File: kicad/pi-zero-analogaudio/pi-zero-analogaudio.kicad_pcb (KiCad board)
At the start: 2 copper layers, 30.5 x 26 mm, 11 parts, among them J2 Pi Connector 2x5 Female, J3 Audio Out, U1 STX-3120-3B

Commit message: drilling holes, silk-screen print
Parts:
- added H1: MountingHole, MountingHole:MountingHole_2.7mm_M2.5_DIN965, F.Cu at (90.5, 62.5)
- added H2: MountingHole, MountingHole:MountingHole_2.7mm_M2.5_DIN965, F.Cu at (114.0, 62.5)
- U1: footprint STX-3120 -> Download:STX-3120
- moved U1 1.28 mm to (114.2, 72.4)
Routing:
- net Net-(C4-Pad2): track 19.9 -> 17.0 mm
- net Net-(C2-Pad2): track 32.5 -> 31.3 mm
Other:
- board text added: "G"
- board text added: "L"
- board text added: "Pi-Zero Audio Rev 6"
- board text added: "R"
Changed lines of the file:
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@@
   (general
     (thickness 1.6)
-    (drawings 4)
-    (tracks 37)
+    (drawings 8)
+    (tracks 35)
     (zones 0)
-    (modules 11)
+    (modules 13)
     (nets 14)
   )
@@
     (add_net "Net-(J2-Pad8)")
     (add_net "Net-(J2-Pad9)")
+  )
+  (module Download:STX-3120 (layer F.Cu)
+    (at 114.2 72.4 180)
+    (fp_text reference U1 (at 0 0) (layer F.SilkS)
+      (effects (font (size 0.787402 0.787402) (thickness 0.015)))
+    )
+    (fp_text value STX-3120-3B (at 0 0) (layer F.Fab)
+      (effects (font (size 0.787402 0.787402) (thickness 0.015)))
+    )
+    (fp_line (start -3 3.4) (end -3 -3.4) (layer F.Fab) (width 0.127))
+    (fp_line (start -6.5 3.4) (end -3 3.4) (layer F.Fab) (width 0.127))
+    (fp_line (start -6.5 -3.4) (end -6.5 3.4) (layer F.Fab) (width 0.127))
+    (fp_line (start -3 -3.4) (end -6.5 -3.4) (layer F.Fab) (width 0.127))
+    (fp_line (start -3 6) (end -3 -6) (layer F.SilkS) (width 0.127))
+    (fp_line (start 8.6 6) (end -3 6) (layer F.SilkS) (width 0.127))
+    (fp_line (start 8.6 -6) (end 8.6 6) (layer F.SilkS) (width 0.127))
+    (fp_line (start -3 -6) (end 8.6 -6) (layer F.SilkS) (width 0.127))
+    (pad None np_thru_hole circle (at 5 0 180) (size 1.6 1.6) (drill 1.6) (layers *.Cu *.Mask))
+    (pad None np_thru_hole circle (at 0 5 180) (size 1.6 1.6) (drill 1.6) (layers *.Cu *.Mask))
+    (pad None np_thru_hole circle (at 0 -5 180) (size 1.6 1.6) (drill 1.6) (layers *.Cu *.Mask))
+    (pad 2 thru_hole circle (at 5 5 180) (size 2.1844 2.1844) (drill 1.3) (layers *.Cu *.Mask)
+      (net 2 "Net-(C2-Pad2)"))
+    (pad 5 thru_hole circle (at 5 -5 180) (size 2.1844 2.1844) (drill 1.3) (layers *.Cu *.Mask)
+      (net 4 "Net-(C4-Pad2)"))
+    (pad 1 thru_hole circle (at 0 0 180) (size 2.1844 2.1844) (drill 1.3) (layers *.Cu *.Mask)
+      (net 13 GND))
+  )
+  (module MountingHole:MountingHole_2.7mm_M2.5_DIN965 (layer F.Cu)
+    (at 114 62.5)
+    (descr "Mounting Hole 2.7mm, no annular, M2.5, DIN965")
+    (tags "mounting hole 2.7mm no annular m2.5 din965")
+    (attr virtual)
+    (fp_text reference H2 (at 0 -3.35) (layer F.SilkS) hide
+      (effects (font (size 1 1) (thickness 0.15)))
+    )
+    (fp_text value MountingHole (at 0 3.35) (layer F.Fab)
+      (effects (font (size 1 1) (thickness 0.15)))
+    )
+    (fp_circle (center 0 0) (end 2.6 0) (layer F.CrtYd) (width 0.05))
+    (fp_circle (center 0 0) (end 2.35 0) (layer Cmts.User) (width 0.15))
+    (fp_text user %R (at 0.3 0) (layer F.Fab)
+      (effects (font (size 1 1) (thickness 0.15)))
+    )
+    (pad 1 np_thru_hole circle (at 0 0) (size 2.7 2.7) (drill 2.7) (layers *.Cu *.Mask))
+  )
+  (module MountingHole:MountingHole_2.7mm_M2.5_DIN965 (layer F.Cu)
+    (at 90.5 62.5)
+    (descr "Mounting Hole 2.7mm, no annular, M2.5, DIN965")
+    (tags "mounting hole 2.7mm no annular m2.5 din965")
+    (zone_connect 0)
+    (attr virtual)
+    (fp_text reference H1 (at 0 -3.35) (layer F.SilkS) hide
+      (effects (font (size 1 1) (thickness 0.15)))
+    )
+    (fp_text value MountingHole (at 0 3.35) (layer F.Fab)
+      (effects (font (size 1 1) (thickness 0.15)))
+    )
+    (fp_circle (center 0 0) (end 2.6 0) (layer F.CrtYd) (width 0.05))
+    (fp_circle (center 0 0) (end 2.35 0) (layer Cmts.User) (width 0.15))
+    (fp_text user %R (at 0.3 0) (layer F.Fab)
+      (effects (font (size 1 1) (thickness 0.15)))
+    )
+    (pad 1 np_thru_hole circle (at 0 0) (size 2.7 2.7) (drill 2.7) (layers *.Cu *.Mask)
+      (zone_connect 0))
   )
   (module Connector_PinHeader_2.54mm:PinHeader_1x03_P2.54mm_Vertical (layer F.Cu)
@@
     )
   )
-  (module STX-3120 (layer F.Cu)
-    (at 114.3 71.12 180)
-    (fp_text reference U1 (at 0 0) (layer F.SilkS)
-      (effects (font (size 0.787402 0.787402) (thickness 0.015)))
-    )
-    (fp_text value STX-3120-3B (at 0 0) (layer F.Fab)
-      (effects (font (size 0.787402 0.787402) (thickness 0.015)))
-    )
-    (fp_line (start -3 -6) (end 8.6 -6) (layer F.SilkS) (width 0.127))
-    (fp_line (start 8.6 -6) (end 8.6 6) (layer F.SilkS) (width 0.127))
-    (fp_line (start 8.6 6) (end -3 6) (layer F.SilkS) (width 0.127))
-    (fp_line (start -3 6) (end -3 -6) (layer F.SilkS) (width 0.127))
-    (fp_line (start -3 -3.4) (end -6.5 -3.4) (layer F.Fab) (width 0.127))
-    (fp_line (start -6.5 -3.4) (end -6.5 3.4) (layer F.Fab) (width 0.127))
-    (fp_line (start -6.5 3.4) (end -3 3.4) (layer F.Fab) (width 0.127))
-    (fp_line (start -3 3.4) (end -3 -3.4) (layer F.Fab) (width 0.127))
-    (pad 1 thru_hole circle (at 0 0 180) (size 2.1844 2.1844) (drill 1.3) (layers *.Cu *.Mask)
-      (net 13 GND))
-    (pad 5 thru_hole circle (at 5 -5 180) (size 2.1844 2.1844) (drill 1.3) (layers *.Cu *.Mask)
-      (net 4 "Net-(C4-Pad2)"))
-    (pad 2 thru_hole circle (at 5 5 180) (size 2.1844 2.1844) (drill 1.3) (layers *.Cu *.Mask)
-      (net 2 "Net-(C2-Pad2)"))
-    (pad None np_thru_hole circle (at 0 -5 180) (size 1.6 1.6) (drill 1.6) (layers *.Cu *.Mask))
-    (pad None np_thru_hole circle (at 0 5 180) (size 1.6 1.6) (drill 1.6) (layers *.Cu *.Mask))
-    (pad None np_thru_hole circle (at 5 0 180) (size 1.6 1.6) (drill 1.6) (layers *.Cu *.Mask))
+  (gr_text G (at 111.8 83.9) (layer F.SilkS)
+    (effects (font (size 1 1) (thickness 0.15)))
+  )
+  (gr_text R (at 114.3 83.8) (layer F.SilkS)
+    (effects (font (size 1 1) (thickness 0.15)))
+  )
+  (gr_text L (at 109.3 83.9) (layer F.SilkS)
+    (effects (font (size 1 1) (thickness 0.15)))
+  )
+  (gr_text "Pi-Zero Audio\nRev 6" (at 111.1 61.6) (layer B.SilkS)
+    (effects (font (size 1 1) (thickness 0.15)) (justify left mirror))
   )
   (gr_line (start 117.5 59) (end 87 59) (layer Edge.Cuts) (width 0.05))
@@
   (segment (start 102.6 67.7) (end 102.8 67.9) (width 0.25) (layer F.Cu) (net 1))
   (segment (start 102.6 63.5) (end 102.6 67.7) (width 0.25) (layer F.Cu) (net 1))
-  (segment (start 103.92 71.5) (end 109.3 66.12) (width 0.25) (layer F.Cu) (net 2))
-  (segment (start 102.7 71.5) (end 103.92 71.5) (width 0.25) (layer F.Cu) (net 2))
-  (segment (start 106.68 63.5) (end 109.3 66.12) (width 0.25) (layer F.Cu) (net 2))
-  (segment (start 104.1 63.5) (end 106.68 63.5) (width 0.25) (layer F.Cu) (net 2))
-  (segment (start 114.28 81.7) (end 112.1 79.52) (width 0.25) (layer F.Cu) (net 2))
-  (segment (start 103.83137 71.5) (end 102.7 71.5) (width 0.25) (layer F.Cu) (net 2))
-  (segment (start 106.777458 71.5) (end 103.83137 71.5) (width 0.25) (layer F.Cu) (net 2))
-  (segment (start 112.1 76.822542) (end 106.777458 71.5) (width 0.25) (layer F.Cu) (net 2))
-  (segment (start 112.1 79.52) (end 112.1 76.822542) (width 0.25) (layer F.Cu) (net 2))
+  (segment (start 113.430001 80.850001) (end 113.430001 80.830001) (width 0.25) (layer F.Cu) (net 2))
+  (segment (start 114.28 81.7) (end 113.430001 80.850001) (width 0.25) (layer F.Cu) (net 2))
+  (segment (start 113.430001 80.830001) (end 111.7 79.1) (width 0.25) (layer F.Cu) (net 2))
+  (segment (start 111.7 69.9) (end 109.2 67.4) (width 0.25) (layer F.Cu) (net 2))
+  (segment (start 111.7 79.1) (end 111.7 69.9) (width 0.25) (layer F.Cu) (net 2))
+  (segment (start 105.1 71.5) (end 109.2 67.4) (width 0.25) (layer F.Cu) (net 2))
+  (segment (start 102.7 71.5) (end 105.1 71.5) (width 0.25) (layer F.Cu) (net 2))
+  (segment (start 105.3 63.5) (end 109.2 67.4) (width 0.25) (layer F.Cu) (net 2))
+  (segment (start 104.1 63.5) (end 105.3 63.5) (width 0.25) (layer F.Cu) (net 2))
   (segment (start 98 78.4) (end 97.7 78.1) (width 0.25) (layer F.Cu) (net 3))
   (segment (start 98 82.1) (end 98 78.4) (width 0.25) (layer F.Cu) (net 3))
   (segment (start 101.7 82.1) (end 101.9 81.9) (width 0.25) (layer F.Cu) (net 3))
   (segment (start 98 82.1) (end 101.7 82.1) (width 0.25) (layer F.Cu) (net 3))
-  (segment (start 109.22 76.2) (end 109.3 76.12) (width 0.25) (layer F.Cu) (net 4))
-  (segment (start 109.22 81.28) (end 109.22 76.2) (width 0.25) (layer F.Cu) (net 4))
-  (segment (start 103.82 76.12) (end 109.3 76.12) (width 0.25) (layer F.Cu) (net 4))
-  (segment (start 102.7 75) (end 103.82 76.12) (width 0.25) (layer F.Cu) (net 4))
-  (segment (start 103.499999 75.799999) (end 102.7 75) (width 0.25) (layer F.Cu) (net 4))
-  (segment (start 103.999999 76.299999) (end 103.499999 75.799999) (width 0.25) (layer F.Cu) (net 4))
-  (segment (start 103.999999 81.300001) (end 103.999999 76.299999) (width 0.25) (layer F.Cu) (net 4))
-  (segment (start 103.4 81.9) (end 103.999999 81.300001) (width 0.25) (layer F.Cu) (net 4))
+  (segment (start 105.1 77.4) (end 109.2 77.4) (width 0.25) (layer F.Cu) (net 4))
+  (segment (start 102.7 75) (end 105.1 77.4) (width 0.25) (layer F.Cu) (net 4))
+  (segment (start 109.2 78.944604) (end 109.2 81.7) (width 0.25) (layer F.Cu) (net 4))
+  (segment (start 109.2 77.4) (end 109.2 78.944604) (width 0.25) (layer F.Cu) (net 4))
+  (segment (start 103.4 79.1) (end 105.1 77.4) (width 0.25) (layer F.Cu) (net 4))
+  (segment (start 103.4 81.9) (end 103.4 79.1) (width 0.25) (layer F.Cu) (net 4))
   (segment (start 90.594999 76.165001) (end 90.920001 75.839999) (width 0.25) (layer F.Cu) (net 10))
   (segment (start 90.594999 80.753631) (end 90.594999 76.165001) (width 0.25) (layer F.Cu) (net 10))

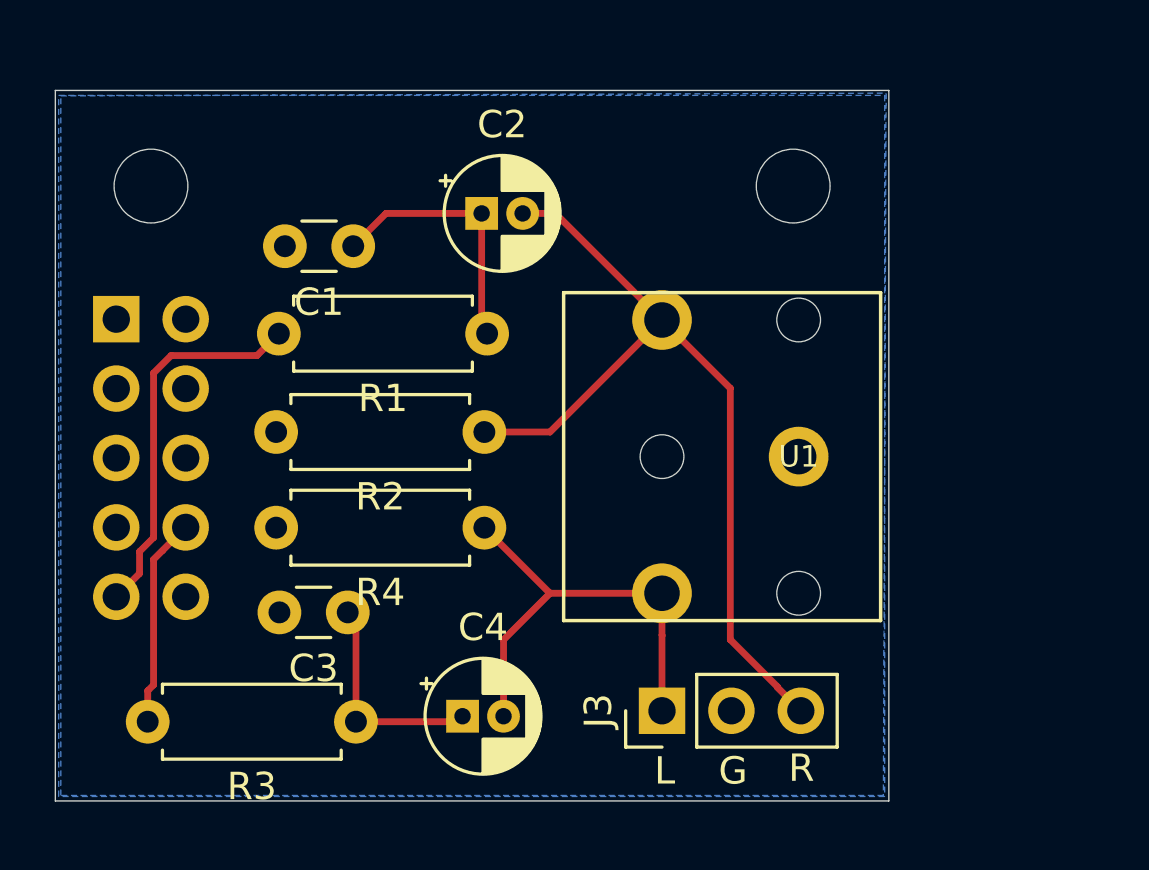
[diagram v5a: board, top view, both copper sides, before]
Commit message: added copper-fill to F.Cu
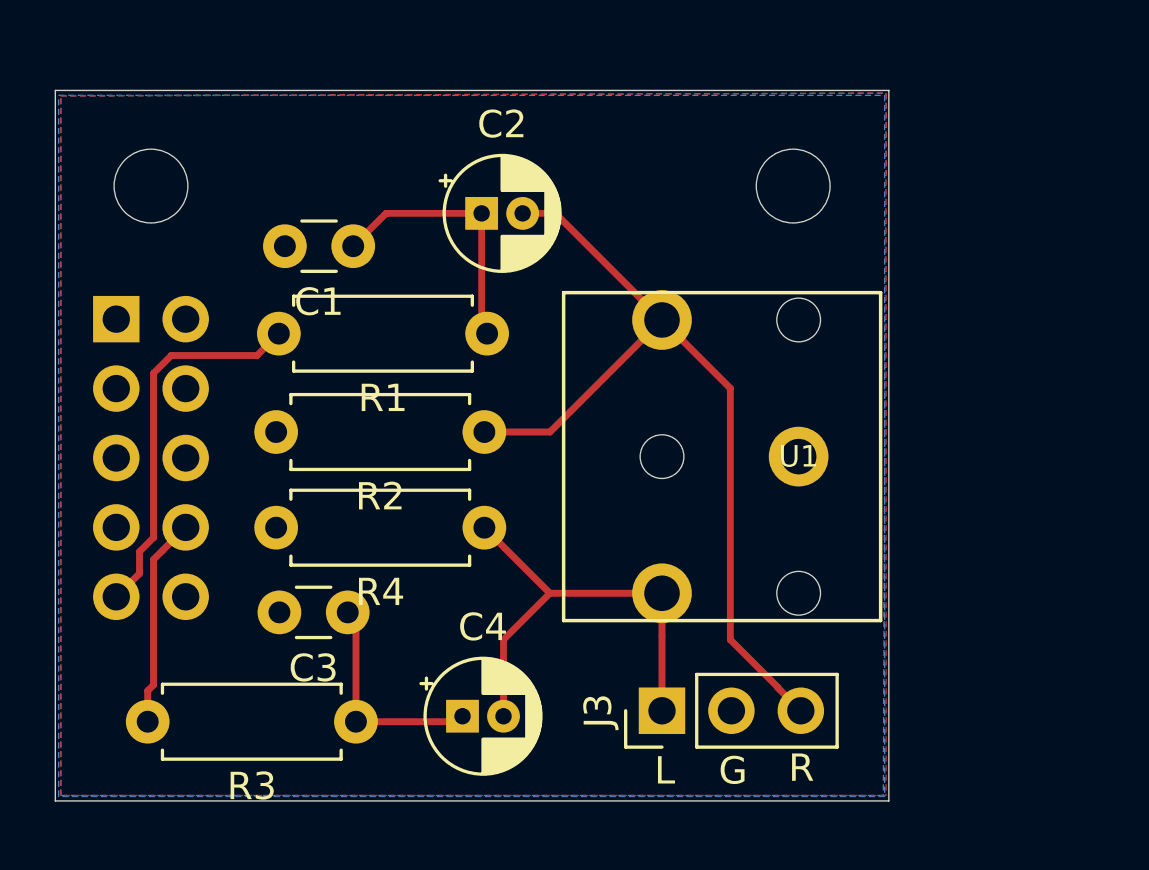
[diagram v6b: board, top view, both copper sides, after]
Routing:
- added copper zone on F.Cu, net GND
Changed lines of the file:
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@@
+    )
+  )
+  (zone (net 13) (net_name GND) (layer F.Cu) (hatch edge 0.508)
+    (connect_pads (clearance 0.508))
+    (min_thickness 0.254)
+    (fill yes (arc_segments 32) (thermal_gap 0.508) (thermal_bridge_width 0.508))
+    (polygon
+      (pts
+        (xy 117.4 84.8) (xy 87.2 84.8) (xy 87.2 59.2) (xy 117.4 59.1)
+      )
     )
   )

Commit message: Revision 7: mounting-hole with pad / small tweaks
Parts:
- H1, H2: footprint MountingHole:MountingHole_2.7mm_M2.5_DIN965 -> MountingHole:MountingHole_2.7mm_M2.5_DIN965_Pad
- renumbered J3 to J1
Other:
- board text added: "Pi-Zero Audio Rev 7"
- board text removed: "Pi-Zero Audio Rev 6"
